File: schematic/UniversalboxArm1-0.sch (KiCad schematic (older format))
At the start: 201 parts, among them J1 USB_B_Micro, J10 Jack-DC, J100 Conn_02x02_Odd_Even, J110 Conn_01x03_Male, J120 Conn_02x04_Counter_Clockwise, J121 Conn_01x02_Male, J20 AVR-ISP-6, J50 Conn_01x14_Female, J60 Conn_01x06_Female, J61 Conn_02x08_Odd_Even, J90 Conn_02x03_Odd_Even, J91 Conn_02x04_Odd_Even, K90 IM01, K91 IM01, K92 IM01, K93 IM01, Q100 BC817, Q101 BC817, Q102 BC817, Q103 BC817, Q120 IRLML6402, Q20 BCX56-16, Q21 BSS138, Q22 BSS138, Q23 IRLML6402, Q24 IRLML6402, Q25 BSS138, Q50 IRLML6402, Q51 IRLML6402, Q52 BSS138, Q60 BSS138, Q61 BSS138, Q62 BSS138, Q90 BSS138, Q91 BSS138, Q92 BSS138, Q93 BSS138, SW60 SW_SPST, SW61 SW_SPST, SW62 SW_SPST, SW63 SW_SPST, U1 USBLC6-2SC6, U10 MCP16301, U100 BD6221F, U101 BD6221F, U110 MAX3221, U130 TSOP312xx, U2 LP38693MP-3.3, U20 ATtiny861A-SU, U21 REF3020, U22 MCP6542, U50 AT45DB641-S, U60 STM32L452RETx, U61 MCP65R41, Y60 16MHz, Y61 32768Hz

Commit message: PCB version 0.2 Use 4 layer instead of 2 layer Remove H-bridge drivers Remove step-down converter
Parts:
- removed C10, C14: 4.7µF, Capacitor_SMD:C_0805_2012Metric_Pad1.15x1.40mm_HandSolder, symbol Device:C
- removed C100, C101, C12, C13: 10µF, Capacitor_SMD:C_0805_2012Metric_Pad1.15x1.40mm_HandSolder, symbol Device:C
- removed C11: 100nF, Capacitor_SMD:C_0805_2012Metric_Pad1.15x1.40mm_HandSolder, symbol Device:C
- removed D10, D101: MBRA340T3G, Diode_SMD:D_SMA, symbol Device:D_Schottky
- removed D100: Z1SMA15, Diode_SMD:D_SMA, symbol Diode:Z1SMAxxx
- removed D11: B140, Diode_SMD:D_SMA, symbol Device:D_Schottky
- removed D12: TS 4148-0805, Diode_SMD:D_0805_2012Metric_Pad1.15x1.40mm_HandSolder, symbol Device:D
- removed D13, D14: SK14, Diode_SMD:D_SMA, symbol Device:D_Schottky
- removed J10: Jack-DC, MalteM:BarrelJack_Horizontal_HEBW21, symbol Connector:Jack-DC
- removed J100: Conn_02x02_Odd_Even, Connector_PinHeader_2.54mm:PinHeader_2x02_P2.54mm_Vertical, symbol Connector_Generic:Conn_02x02_Odd_Even
- removed L10: 22µH, Inductor_SMD:L_6.3x6.3_H3, symbol Device:L
- removed Q100, Q101, Q102, Q103: BC817, Package_TO_SOT_SMD:SOT-23, symbol Transistor_BJT:BC817
- removed Q52: BSS138, Package_TO_SOT_SMD:SOT-23, symbol Transistor_FET:BSS138
- removed R10: 56kΩ, Resistor_SMD:R_0805_2012Metric_Pad1.15x1.40mm_HandSolder, symbol Device:R
- removed R100, R101, R102, R103: 1kΩ, Resistor_SMD:R_0805_2012Metric_Pad1.15x1.40mm_HandSolder, symbol Device:R
- removed R105, R106, R107, R108, R11: 10kΩ, Resistor_SMD:R_0805_2012Metric_Pad1.15x1.40mm_HandSolder, symbol Device:R
- removed R54: 220kΩ, Resistor_SMD:R_0805_2012Metric_Pad1.15x1.40mm_HandSolder, symbol Device:R
- removed TP10: TestPoint, TestPoint:TestPoint_THTPad_D1.5mm_Drill0.7mm, symbol Connector:TestPoint
- removed U10: MCP16301, Package_TO_SOT_SMD:SOT-23-6, symbol Regulator_Switching:MCP16301
- removed U100, U101: BD6221F, Package_SO:SOIC-8_3.9x4.9mm_P1.27mm, symbol RohmMotorDrivers:BD6221F
- added H4: MountingHole_Pad, MountingHole:MountingHole_3.2mm_M3_Pad, symbol Mechanical:MountingHole_Pad
- added J62: Conn_02x04_Odd_Even, Connector_PinHeader_2.54mm:PinHeader_2x04_P2.54mm_Vertical, symbol Connector_Generic:Conn_02x04_Odd_Even
- added JP61: SolderJumper_2_Open, Jumper:SolderJumper-2_P1.3mm_Open_RoundedPad1.0x1.5mm, symbol Jumper:SolderJumper_2_Open
- D60, D61: symbol Device:LED_Dual_ACA -> UniversalboxArm1-0-rescue:LED_Dual_ACA-Device
- J1: symbol Connector:USB_B_Micro -> UniversalboxArm1-0-rescue:USB_B_Micro-Connector
- J20: symbol Connector:AVR-ISP-6 -> UniversalboxArm1-0-rescue:AVR-ISP-6-Connector
- U1: symbol Power_Protection:USBLC6-2SC6 -> UniversalboxArm1-0-rescue:USBLC6-2SC6-Power_Protection
- U20: symbol MCU_Microchip_ATtiny:ATtiny861A-SU -> UniversalboxArm1-0-rescue:ATtiny861A-SU-MCU_Microchip_ATtiny
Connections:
- net labels added: DisablePower, IrRec, VccBase
- net labels removed: +VDC
- wire segments 846 -> 750
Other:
- note added: "2. connector and relais output"
- note added: "BP+"
- note added: "BP-"
- note added: "Checked for the STM32L45xxx:\nBP+: Bootloader drives this pin as pull-up\nBP-: Bootloader drives this pin as pull-down"
- note removed: "7.5-14V DC"
- note removed: "C10, C14, 25V variant"
- note removed: "H-bridge and relais output"
- note removed: "H-bridge drivers support 20kHz...100kHz PWM"
- note removed: "Needed to limit inducted voltage\nby braking motors"
- note removed: "Vout=5.28V"
- moved on the sheet: C1, C2, D90, D91, D92, D93, J90, J91, JP90, JP91, JP92, JP93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

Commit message: Revision - 0.3. Send to production.
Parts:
- added C4: 100µF, Capacitor_SMD:C_1206_3216Metric_Pad1.33x1.80mm_HandSolder, symbol Device:C
- added D3: SK14, Diode_SMD:D_SMA, symbol Device:D_Schottky
- added H5: MountingHole_Pad, MountingHole:MountingHole_3.2mm_M3_Pad, symbol Mechanical:MountingHole_Pad
- C120: footprint Capacitor_SMD:C_1206_3216Metric_Pad1.42x1.75mm_HandSolder -> Capacitor_SMD:C_1206_3216Metric_Pad1.33x1.80mm_HandSolder
- C3: renamed from C121; footprint Capacitor_SMD:C_1206_3216Metric_Pad1.42x1.75mm_HandSolder -> Capacitor_SMD:C_1206_3216Metric_Pad1.33x1.80mm_HandSolder
- U110: footprint Package_SO:SSOP-16_5.3x6.2mm_P0.65mm -> MalteM:SSOP-16_5.3x6.2mm_P0.65mm_Handsolder
- U60: footprint Package_QFP:LQFP-64_10x10mm_P0.5mm -> MalteM:LQFP-64_10x10mm_P0.5mm_Handsoldering
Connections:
- net labels added: FlashCS, KeyDown, KeyLeft, KeyRight, KeyUp
- wire segments 750 -> 759
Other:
- note added: "Close JP61 if U130 is used"
- note added: "Display RAM requirements"
- note added: "Optional"
- note removed: "Display RAM Requirements"
- moved on the sheet: C3
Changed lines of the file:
@@
 Sheet 1 1
 Title ""
-Date "2021-11-05"
-Rev "0.2"
+Date "2021-11-10"
+Rev "0.3"
 Comp ""
 Comment1 ""
@@
 F 0 "U60" H 4400 10114 50  0000 C CNN
 F 1 "STM32L452RETx" H 4400 10023 50  0000 C CNN
-F 2 "Package_QFP:LQFP-64_10x10mm_P0.5mm" H 3850 10300 50  0001 R CNN
+F 2 "MalteM:LQFP-64_10x10mm_P0.5mm_Handsoldering" H 3850 10300 50  0001 R CNN
 F 3 "http://www.st.com/st-web-ui/static/active/en/resource/technical/document/datasheet/DM00340549.pdf" H 4450 12000 50  0001 C CNN
 	1    4450 12000
@@
 	1    0    0    -1
 $EndComp
-Text Label 13500 2900 0    50   ~ 0
-Motor1R
 Text Label 13500 3200 0    50   ~ 0
+Motor1R
+Text Label 13500 2900 0    50   ~ 0
 Motor1F
 Text Label 13500 5400 0    50   ~ 0
@@
 Text Label 7950 13700 0    50   ~ 0
 AvrSck
-NoConn ~ 2750 2800
-Wire Wire Line
-	2750 2800 2750 2900
 $Comp
 L Interface_UART:MAX3221 U110
@@
 F 0 "U110" H 19500 10928 50  0000 C CNN
 F 1 "MAX3221" H 19500 10837 50  0000 C CNN
-F 2 "Package_SO:SSOP-16_5.3x6.2mm_P0.65mm" H 19550 9850 50  0001 C CIN
+F 2 "MalteM:SSOP-16_5.3x6.2mm_P0.65mm_Handsolder" H 19550 9850 50  0001 C CIN
 F 3 "http://www.ti.com/lit/ds/symlink/max3221.pdf" H 19500 10800 50  0001 C CNN
 	1    19500 9850
@@
 Placeholder for\ndimensions of\n160x128 LCD
 Wire Wire Line
-	3750 13400 3650 13400
-Wire Wire Line
 	7500 13500 8250 13500
 Wire Wire Line
@@
 Text Label 3300 13100 0    50   ~ 0
 SpiAvrSck
-Wire Wire Line
-	3650 13400 3650 14450
 $Comp
 L Device:Crystal Y60
@@
 	1    0    0    -1
 $EndComp
-$Comp
-L Device:Crystal Y61
-U 1 1 6146543E
-P 3100 11450
-F 0 "Y61" V 3054 11581 50  0000 L CNN
-F 1 "32768Hz" V 3145 11581 50  0000 L CNN
-F 2 "MalteM:Crystal_MP03" H 3100 11450 50  0001 C CNN
-F 3 "~" H 3100 11450 50  0001 C CNN
-	1    3100 11450
-	0    -1   -1   0
-$EndComp
 Wire Wire Line
 	3750 11500 3550 11500
@@
 	5050 13600 6000 13600
 Wire Wire Line
-	3650 14450 7500 14450
-Wire Wire Line
 	5050 13000 7600 13000
 Wire Wire Line
@@
 USART1
 Text Notes 21350 12300 0    50   ~ 0
-Display RAM Requirements
+Display RAM requirements
 Text Notes 20950 12600 0    50   ~ 0
 128x128
@@
 F 0 "C120" H 14565 9896 50  0000 L CNN
 F 1 "100µF" H 14565 9805 50  0000 L CNN
-F 2 "Capacitor_SMD:C_1206_3216Metric_Pad1.42x1.75mm_HandSolder" H 14488 9700 50  0001 C CNN
+F 2 "Capacitor_SMD:C_1206_3216Metric_Pad1.33x1.80mm_HandSolder" H 14488 9700 50  0001 C CNN
 F 3 "~" H 14450 9850 50  0001 C CNN
 	1    14450 9850
@@
 	14450 9600 14250 9600
 $Comp
-L Device:C C121
+L Device:C C3
 U 1 1 6310D4BD
-P 13200 9750
-F 0 "C121" H 13315 9796 50  0000 L CNN
-F 1 "100µF" H 13315 9705 50  0000 L CNN
-F 2 "Capacitor_SMD:C_1206_3216Metric_Pad1.42x1.75mm_HandSolder" H 13238 9600 50  0001 C CNN
-F 3 "~" H 13200 9750 50  0001 C CNN
-	1    13200 9750
-	1    0    0    -1
-$EndComp
-$Comp
-L power:GND #PWR0192
-U 1 1 6310D919
-P 13200 9950
-F 0 "#PWR0192" H 13200 9700 50  0001 C CNN
-F 1 "GND" H 13205 9777 50  0000 C CNN
-F 2 "" H 13200 9950 50  0001 C CNN
-F 3 "" H 13200 9950 50  0001 C CNN
-	1    13200 9950
+P 11250 2250
+F 0 "C3" H 11365 2296 50  0000 L CNN
+F 1 "100µF" H 11365 2205 50  0000 L CNN
+F 2 "Capacitor_SMD:C_1206_3216Metric_Pad1.33x1.80mm_HandSolder" H 11288 2100 50  0001 C CNN
+F 3 "~" H 11250 2250 50  0001 C CNN
+	1    11250 2250
 	1    0    0    -1
 $EndComp
 Wire Wire Line
 	13850 9600 13600 9600
-Wire Wire Line
-	13200 9900 13200 9950
 $Comp
 L Device:R R120
@@
 	1    0    0    -1
 $EndComp
-Connection ~ 13200 9600
 Wire Wire Line
 	15400 9500 15750 9500
@@
 F 3 "http://www.littelfuse.com/~/media/files/littelfuse/technical%20resources/documents/data%20sheets/sp05xxba.pdf" H 15375 14325 50  0001 C CNN
 	1    15250 14200
-	-1   0    0    -1
+	1    0    0    -1
 $EndComp
 Wire Wire Line
@@
 Wire Wire Line
 	15350 3650 15350 3500
-Wire Wire Line
-	3900 1400 9300 1400
 Text Label 5350 1400 0    50   ~ 0
 VccBase
@@
 Text Label 7350 12300 0    50   ~ 0
 IrRec
+Wire Wire Line
+	10800 2100 11250 2100
+Wire Wire Line
+	11250 2400 10800 2400
+Connection ~ 10800 2400
+Text Notes 11300 2100 0    50   ~ 0
+Optional
+$Comp
+L Device:C C4
+U 1 1 61AC88C7
+P 8500 1550
+F 0 "C4" H 8615 1596 50  0000 L CNN
+F 1 "100µF" H 8615 1505 50  0000 L CNN
+F 2 "Capacitor_SMD:C_1206_3216Metric_Pad1.33x1.80mm_HandSolder" H 8538 1400 50  0001 C CNN
+F 3 "~" H 8500 1550 50  0001 C CNN
+	1    8500 1550
+	1    0    0    -1
+$EndComp
+Connection ~ 8500 1400
+Wire Wire Line
+	8500 1400 9300 1400
+Text Notes 8400 1300 0    50   ~ 0
+Optional
+$Comp
+L power:GND #PWR0108
+U 1 1 61AC92A7
+P 8500 1850
+F 0 "#PWR0108" H 8500 1600 50  0001 C CNN
+F 1 "GND" H 8505 1677 50  0000 C CNN
+F 2 "" H 8500 1850 50  0001 C CNN
+F 3 "" H 8500 1850 50  0001 C CNN
+	1    8500 1850
+	1    0    0    -1
+$EndComp
+Wire Wire Line
+	8500 1850 8500 1700
+Wire Wire Line
+	2750 2800 2750 2900
+NoConn ~ 2750 2800
+Wire Wire Line
+	3900 1400 5900 1400
+$Comp
+L Device:D_Schottky D3
+U 1 1 61B9C9A3
+P 5100 1050
+F 0 "D3" H 5100 834 50  0000 C CNN
+F 1 "SK14" H 5100 925 50  0000 C CNN
+F 2 "Diode_SMD:D_SMA" H 5100 1050 50  0001 C CNN
+F 3 "~" H 5100 1050 50  0001 C CNN
+	1    5100 1050
+	-1   0    0    1
+$EndComp
+Wire Wire Line
+	5250 1050 5900 1050
+Wire Wire Line
+	5900 1050 5900 1400
+Connection ~ 5900 1400
+Wire Wire Line
+	5900 1400 8500 1400
+Wire Wire Line
+	4400 1050 4950 1050
+Connection ~ 4400 1050
+$Comp
+L Mechanical:MountingHole_Pad H5
+U 1 1 61F5568B
+P 10300 8000
+F 0 "H5" H 10200 7958 50  0000 R CNN
+F 1 "MountingHole_Pad" H 10200 8049 50  0000 R CNN
+F 2 "MountingHole:MountingHole_3.2mm_M3_Pad" H 10300 8000 50  0001 C CNN
+F 3 "~" H 10300 8000 50  0001 C CNN
+	1    10300 8000
+	-1   0    0    1
+$EndComp
+Wire Wire Line
+	10650 7750 10300 7750
+Wire Wire Line
+	10300 7750 10300 7900
+Connection ~ 10650 7750
+Text Label 3350 12500 0    50   ~ 0
+FlashCS
+Text Label 5250 11900 0    50   ~ 0
+KeyLeft
+Text Label 5250 13000 0    50   ~ 0
+KeyRight
+Text Label 3300 12900 0    50   ~ 0
+KeyDown
+Wire Wire Line
+	2700 13400 2700 14450
+Wire Wire Line
+	2700 13400 3750 13400
+Wire Wire Line
+	2700 14450 7500 14450
+Text Label 3300 13400 0    50   ~ 0
+KeyUp
+Text Notes 7450 12200 0    50   ~ 0
+Close JP61 if U130 is used
+$Comp
+L Device:Crystal Y61
+U 1 1 6146543E
+P 3100 11450
+F 0 "Y61" V 3054 11581 50  0000 L CNN
+F 1 "32768Hz" V 3145 11581 50  0000 L CNN
+F 2 "MalteM:Crystal_MP03" H 3100 11450 50  0001 C CNN
+F 3 "~" H 3100 11450 50  0001 C CNN
+	1    3100 11450
+	0    -1   -1   0
+$EndComp
 $EndSCHEMATC

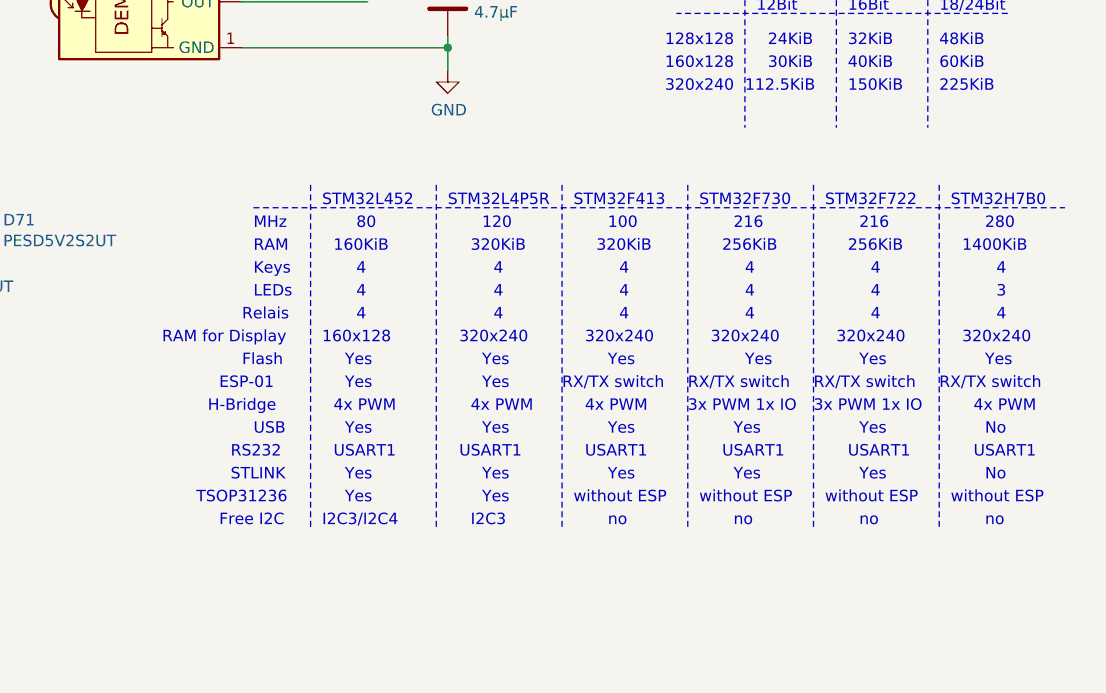
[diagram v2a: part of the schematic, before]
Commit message: Update BOM and pin usage restrictions.
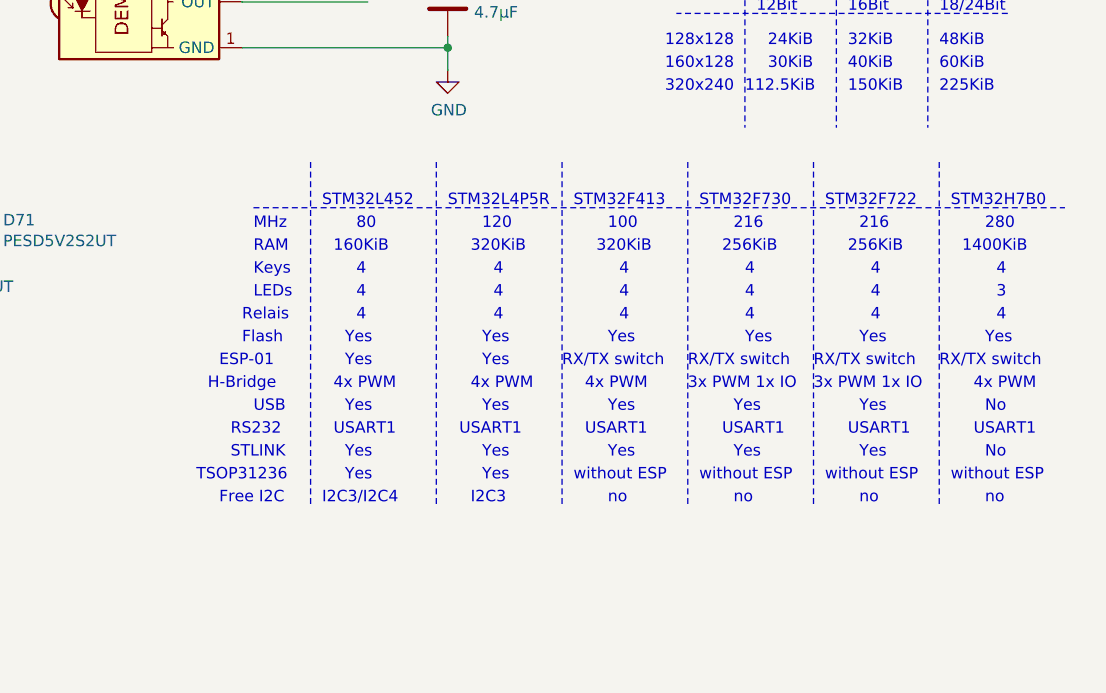
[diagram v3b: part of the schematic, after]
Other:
- note removed: "RAM for Display"
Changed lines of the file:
@@
 Sheet 1 1
 Title ""
-Date "2021-11-10"
+Date "2021-11-13"
 Rev "0.3"
 Comp ""
@@
 Text Notes 19100 13800 0    50   ~ 0
 Relais
-Text Notes 18750 13900 0    50   ~ 0
-RAM for Display
-Text Notes 19100 14000 0    50   ~ 0
+Text Notes 19100 13900 0    50   ~ 0
 Flash
-Text Notes 19000 14100 0    50   ~ 0
+Text Notes 19000 14000 0    50   ~ 0
 ESP-01
-Text Notes 18950 14200 0    50   ~ 0
+Text Notes 18950 14100 0    50   ~ 0
 H-Bridge
-Text Notes 19150 14300 0    50   ~ 0
+Text Notes 19150 14200 0    50   ~ 0
 USB
 Text Notes 19600 13600 0    50   ~ 0
@@
 Text Notes 22250 13500 0    50   ~ 0
 1400KiB
-Text Notes 19550 14000 0    50   ~ 0
+Text Notes 19550 13900 0    50   ~ 0
 Yes
-Text Notes 20700 14000 0    50   ~ 0
+Text Notes 20700 13900 0    50   ~ 0
 Yes
-Text Notes 21800 14000 0    50   ~ 0
+Text Notes 21800 13900 0    50   ~ 0
 Yes
-Text Notes 22350 14000 0    50   ~ 0
+Text Notes 22350 13900 0    50   ~ 0
 Yes
-Text Notes 19450 13900 0    50   ~ 0
-160x128
-Text Notes 21700 13900 0    50   ~ 0
-320x240
-Text Notes 22250 13900 0    50   ~ 0
-320x240
-Text Notes 19550 14100 0    50   ~ 0
+Text Notes 19550 14000 0    50   ~ 0
 Yes
-Text Notes 20500 14100 0    50   ~ 0
+Text Notes 20500 14000 0    50   ~ 0
 RX/TX switch
-Text Notes 21600 14100 0    50   ~ 0
+Text Notes 21600 14000 0    50   ~ 0
 RX/TX switch
-Text Notes 22150 14100 0    50   ~ 0
+Text Notes 22150 14000 0    50   ~ 0
 RX/TX switch
-Text Notes 19500 14200 0    50   ~ 0
+Text Notes 19500 14100 0    50   ~ 0
 4x PWM
-Text Notes 19550 14300 0    50   ~ 0
+Text Notes 19550 14200 0    50   ~ 0
 Yes
-Text Notes 20700 14300 0    50   ~ 0
+Text Notes 20700 14200 0    50   ~ 0
 Yes
-Text Notes 21800 14300 0    50   ~ 0
+Text Notes 21800 14200 0    50   ~ 0
 Yes
-Text Notes 22350 14300 0    50   ~ 0
+Text Notes 22350 14200 0    50   ~ 0
 No
-Text Notes 20600 14200 0    50   ~ 0
+Text Notes 20600 14100 0    50   ~ 0
 4x PWM
-Text Notes 22300 14200 0    50   ~ 0
+Text Notes 22300 14100 0    50   ~ 0
 4x PWM
-Text Notes 21600 14200 0    50   ~ 0
+Text Notes 21600 14100 0    50   ~ 0
 3x PWM 1x IO
-Text Notes 20600 13900 0    50   ~ 0
-320x240
-Text Notes 19050 14400 0    50   ~ 0
+Text Notes 19050 14300 0    50   ~ 0
 RS232
-Text Notes 21750 14400 0    50   ~ 0
+Text Notes 21750 14300 0    50   ~ 0
 USART1
-Text Notes 20600 14400 0    50   ~ 0
+Text Notes 20600 14300 0    50   ~ 0
 USART1
-Text Notes 22300 14400 0    50   ~ 0
+Text Notes 22300 14300 0    50   ~ 0
 USART1
 Text Notes 21350 12300 0    50   ~ 0
@@
 Text Notes 22150 12800 0    50   ~ 0
 225KiB
-Text Notes 19050 14500 0    50   ~ 0
+Text Notes 19050 14400 0    50   ~ 0
 STLINK
-Text Notes 19550 14500 0    50   ~ 0
+Text Notes 19550 14400 0    50   ~ 0
 Yes
-Text Notes 20700 14500 0    50   ~ 0
+Text Notes 20700 14400 0    50   ~ 0
 Yes
-Text Notes 21800 14500 0    50   ~ 0
+Text Notes 21800 14400 0    50   ~ 0
 Yes
-Text Notes 22350 14500 0    50   ~ 0
+Text Notes 22350 14400 0    50   ~ 0
 No
 Text Notes 21100 13300 0    50   ~ 0
@@
 Text Notes 20100 13500 0    50   ~ 0
 320KiB
-Text Notes 20050 13900 0    50   ~ 0
-320x240
-Text Notes 21150 13900 0    50   ~ 0
-320x240
 Wire Wire Line
 	14450 9400 14450 9500
@@
 Wire Wire Line
 	3300 9900 3300 12200
-Text Notes 18900 14600 0    50   ~ 0
+Text Notes 18900 14500 0    50   ~ 0
 TSOP31236
-Text Notes 19550 14600 0    50   ~ 0
+Text Notes 19550 14500 0    50   ~ 0
 Yes
-Text Notes 20550 14600 0    50   ~ 0
+Text Notes 20550 14500 0    50   ~ 0
 without ESP
-Text Notes 21650 14600 0    50   ~ 0
+Text Notes 21650 14500 0    50   ~ 0
 without ESP
-Text Notes 22200 14600 0    50   ~ 0
+Text Notes 22200 14500 0    50   ~ 0
 without ESP
 Wire Wire Line
@@
 Text Label 19550 11550 0    50   ~ 0
 ADC3
-Text Notes 20050 14400 0    50   ~ 0
+Text Notes 20050 14300 0    50   ~ 0
 USART1
-Text Notes 19500 14400 0    50   ~ 0
+Text Notes 19500 14300 0    50   ~ 0
 USART1
-Text Notes 20150 14500 0    50   ~ 0
+Text Notes 20150 14400 0    50   ~ 0
 Yes
-Text Notes 20150 14600 0    50   ~ 0
+Text Notes 20150 14500 0    50   ~ 0
 Yes
-Text Notes 20150 14300 0    50   ~ 0
+Text Notes 20150 14200 0    50   ~ 0
 Yes
-Text Notes 20100 14200 0    50   ~ 0
+Text Notes 20100 14100 0    50   ~ 0
 4x PWM
-Text Notes 20150 14100 0    50   ~ 0
-Yes
 Text Notes 20150 14000 0    50   ~ 0
 Yes
+Text Notes 20150 13900 0    50   ~ 0
+Yes
 Text Notes 20200 13800 0    50   ~ 0
 4
@@
 Text Notes 20200 13600 0    50   ~ 0
 4
-Text Notes 21050 14200 0    50   ~ 0
-3x PWM 1x IO
 Text Notes 21050 14100 0    50   ~ 0
+3x PWM 1x IO
+Text Notes 21050 14000 0    50   ~ 0
 RX/TX switch
-Text Notes 21250 14300 0    50   ~ 0
+Text Notes 21250 14200 0    50   ~ 0
 Yes
-Text Notes 21200 14400 0    50   ~ 0
+Text Notes 21200 14300 0    50   ~ 0
 USART1
-Text Notes 21250 14500 0    50   ~ 0
+Text Notes 21250 14400 0    50   ~ 0
 Yes
-Text Notes 21100 14600 0    50   ~ 0
+Text Notes 21100 14500 0    50   ~ 0
 without ESP
-Text Notes 21300 14000 0    50   ~ 0
+Text Notes 21300 13900 0    50   ~ 0
 Yes
 Text Notes 21300 13800 0    50   ~ 0
@@
 Text Notes 2950 12150 0    50   ~ 0
 or I2C
-Text Notes 19000 14700 0    50   ~ 0
+Text Notes 19000 14600 0    50   ~ 0
 Free I2C
-Text Notes 21800 14700 0    50   ~ 0
+Text Notes 21800 14600 0    50   ~ 0
 no
-Text Notes 19450 14700 0    50   ~ 0
+Text Notes 19450 14600 0    50   ~ 0
 I2C3/I2C4
-Text Notes 20100 14700 0    50   ~ 0
+Text Notes 20100 14600 0    50   ~ 0
 I2C3
-Text Notes 20700 14700 0    50   ~ 0
+Text Notes 20700 14600 0    50   ~ 0
 no
 Wire Notes Line
-	19400 13200 19400 14700
+	19400 13100 19400 14600
 Wire Notes Line
-	19950 13200 19950 14700
+	19950 13100 19950 14600
 Wire Notes Line
-	20500 13200 20500 14700
+	20500 13100 20500 14600
 Wire Notes Line
-	21050 13200 21050 14700
+	21050 13100 21050 14600
 Wire Notes Line
-	21600 13200 21600 14700
+	21600 13100 21600 14600
 Wire Notes Line
-	22150 13200 22150 14700
-Text Notes 22350 14700 0    50   ~ 0
+	22150 13100 22150 14600
+Text Notes 22350 14600 0    50   ~ 0
 no
-Text Notes 21250 14700 0    50   ~ 0
+Text Notes 21250 14600 0    50   ~ 0
 no
 Wire Wire Line

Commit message: Update schematic, replace resistor by diode Also make the schematic more easy to read
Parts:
- R62, R64: value 330Ω -> 180Ω
- U61: value MCP65R41 -> MCP65R41T-1202E
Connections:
- net labels added: DIODE, Led2Red, Led2green
- wire segments 759 -> 756
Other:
- note added: "0.5% tolerance of D22 should limit \nVbattery to 3.509V ... 3.544V"
- note added: "Always block if on\nUSB power\nAVR can only enable if on\nbattery power\n"
- note added: "Bug: TH20 is connected to a digital I/O."
- note added: "H-Bridges as\nextension PCB"
- note added: "J62"
- note added: "Norm:\nVin=4.5V, vout=3.3V\nmax 300mA\n-> (4.5-3.3)/0.3=4Ω\nMax: 5V-3V=2V\nP_Q20=2V*0.3A=0.6W"
- note added: "P_R20_min=0.5W"
- note added: "Part naming conventions:\n*0..*9: USB Vin\n*10...*19: reserved\n*20...*49: Battery Vin\n*50...*59: LCD and flash\n*60...*89: ARM CPU + basics\n*90...*99: Relais\n*100...*109: Reserved\n*110...*119: RS232\n*120...*129: ESP-01\n*130...*139: TSOP31236"
- note added: "Replace R31 by Diode\nTS4148 RY"
- note added: "STM32L496"
- note added: "green"
- note added: "use 0.5% precision\nvariant for D22,\nlike TS431BCX\n"
- note removed: "0.5% tolerance should limit between\n3.509V and 3.544V"
- note removed: "Always block if on\nUSB or Jack-DC power\nAVR can only enable if on\nbattery power\n"
- note removed: "H-Bridge"
- note removed: "Norm:\nVin=4.5V, vout=3.3V\nmax 300mA\n-> (4.5-3.3)/0.3=4Ω\nMax: 5V-3V=2V\n2V*0.3A = 0.6W"
- note removed: "Part naming conventions:\n*0..*9: USB Vin\n*10...*19: DC Jack Vin\n*20...*49: Battery Vin\n*50...*59: LCD and flash\n*60...*89: ARM CPU + basics\n*90...*99: Relais\n*100...*109: Motor drivers\n*110...*119: RS232\n*120...*129: ESP-01\n*130...*139: TSOP31236"
- note removed: "min 0.5W"
- note removed: "use 0.5% precision\nvariant,\nlike TS431BCX\n"
- moved on the sheet: BT20, C2, C23, C24, C3, D20, D21, D22, D23, D24, F20, JP1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
